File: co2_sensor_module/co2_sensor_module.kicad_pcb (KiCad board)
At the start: 2 copper layers, 85 x 55 mm, 59 parts, among them J1 Conn_ARM_SWD_TagConnect_TC203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, J2 Conn_01x04, J3 Conn_01x04, J4 Conn_01x03, J5 Conn_01x04, SW1 SW_DIP_x04, U1 SGX-7OX, U10 TPS62125DSG, U2 CBLW 24C02, U3 ADS1115IDGS, U4 TPS62125DSG, U5 MS5611-01BA, U6 SHT4x, U7 STC31-C, U8 TJA1042T-3, U9 STM32L432KBUx

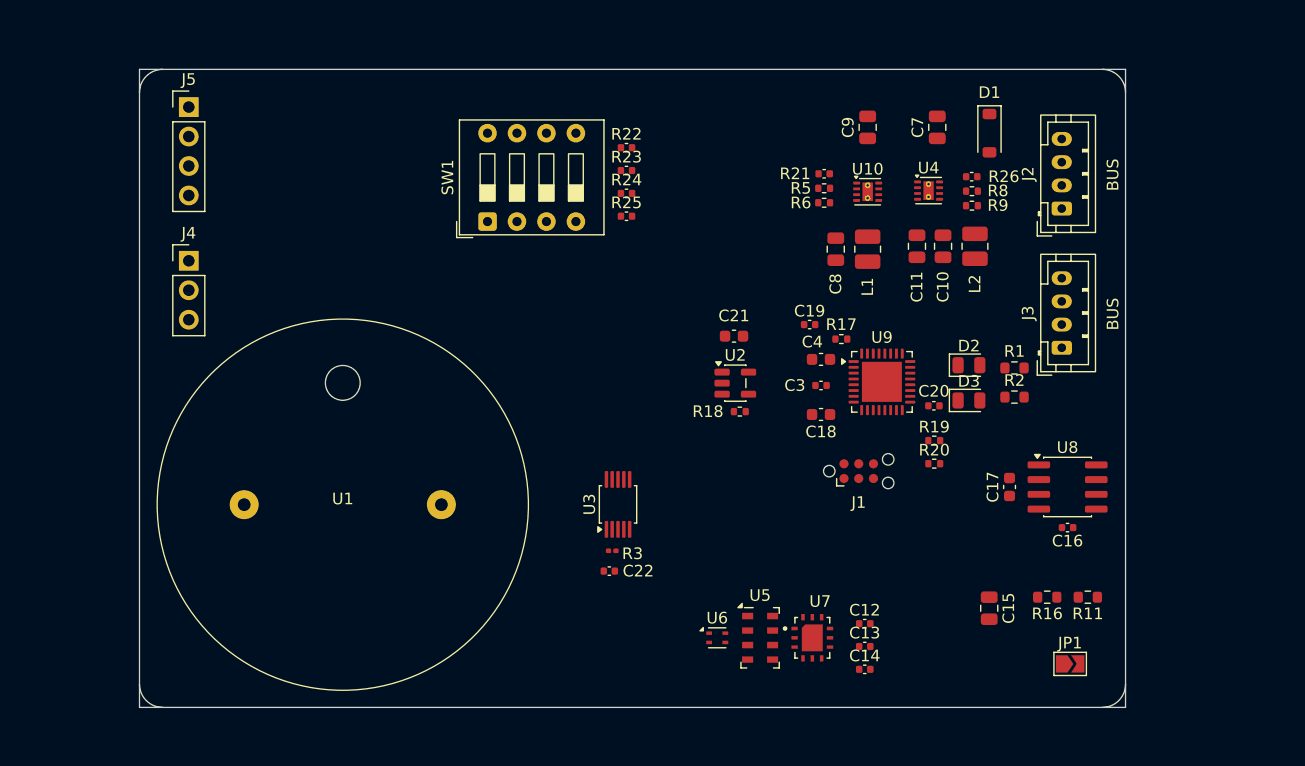
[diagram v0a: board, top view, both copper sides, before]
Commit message: some work on layout for co2 sensor unit
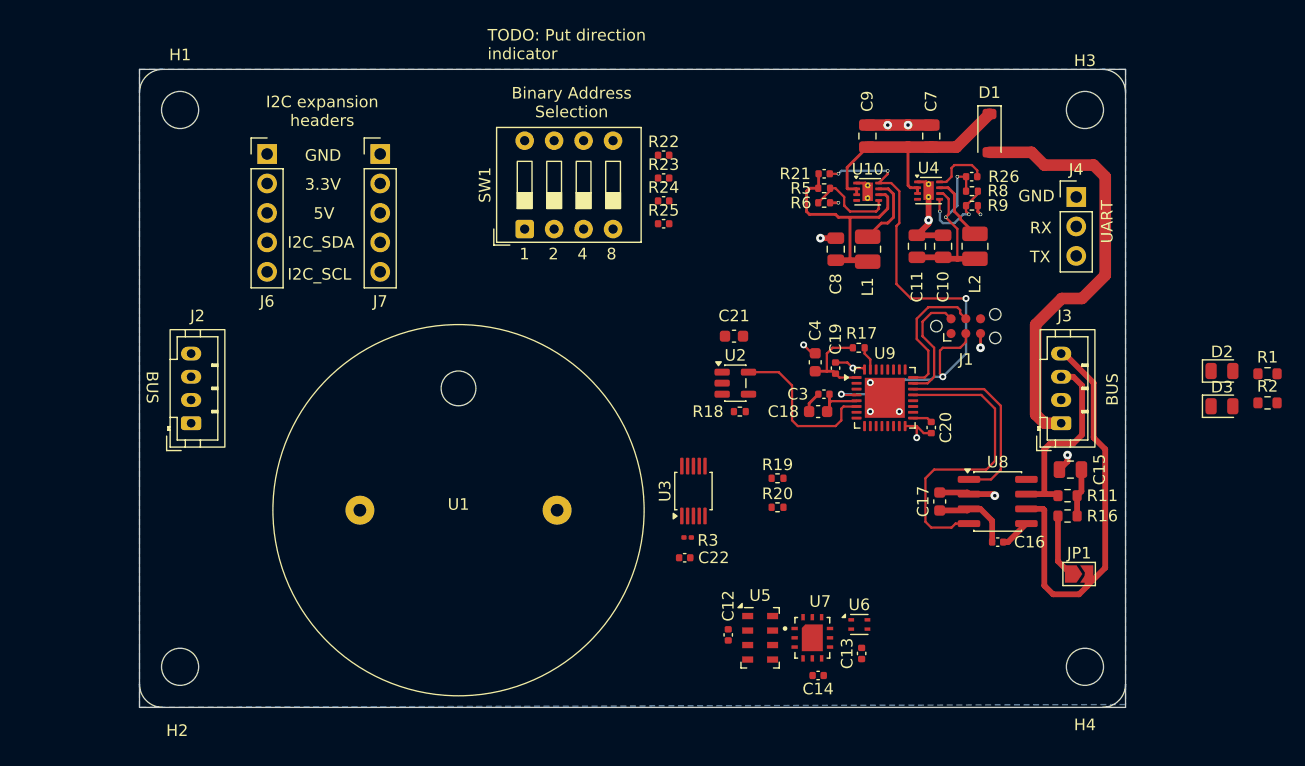
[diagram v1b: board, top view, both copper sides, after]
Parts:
- removed J5: Conn_01x04, Connector_PinHeader_2.54mm:PinHeader_1x04_P2.54mm_Vertical
- added H1: MountingHole 3M, MountingHole:MountingHole_3.2mm_M3, F.Cu at (99.5, 66.5)
- added H2: MountingHole 3M, MountingHole:MountingHole_3.2mm_M3, F.Cu at (99.5, 114.5)
- added H3: MountingHole 3M, MountingHole:MountingHole_3.2mm_M3, F.Cu at (177.5, 66.5)
- added H4: MountingHole 3M, MountingHole:MountingHole_3.2mm_M3, F.Cu at (177.5, 114.5)
- added J6: Conn_01x05, Connector_PinHeader_2.54mm:PinHeader_1x05_P2.54mm_Vertical, F.Cu at (107.0, 70.3)
- added J7: Conn_01x05, Connector_PinHeader_2.54mm:PinHeader_1x05_P2.54mm_Vertical, F.Cu at (116.8, 70.3)
- moved J2 77.3 mm to (100.5, 93.5)
- moved J4 76.7 mm to (176.8, 74.0)
- moved D2 21.8 mm to (189.3, 89.0)
- moved D3 21.8 mm to (189.3, 92.0)
- moved R1 21.8 mm to (193.2, 89.2)
- moved R2 21.8 mm to (193.2, 91.8)
- moved J1 15.5 mm to (167.2, 85.1)
- moved R20 14.0 mm to (151.0, 100.8)
- moved R19 13.9 mm to (151.0, 98.2)
- moved C15 13.8 mm to (176.2, 97.5), turned to 180 degrees
- moved U6 12.3 mm to (158.1, 110.8)
- moved C12 11.8 mm to (146.8, 111.8), turned to -90 degrees
- moved U1 9.99 mm to (123.5, 101.0)
- moved R11 8.92 mm to (176.0, 99.8), turned to 0 degrees
- moved JP1 7.79 mm to (177.0, 106.5)
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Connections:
- net /CAN/PV50 renamed /P5V0
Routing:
- net /MCU/~{nRST}: track 0.00 -> 47.1 mm, vias 0 -> 5
- net /Vbus: track 0.00 -> 37.4 mm
- net /P3V3: track 0.00 -> 36.1 mm
- net /CANL: track 0.00 -> 35.8 mm
- net /GND: track 0.00 -> 33.2 mm, vias 0 -> 15
- net /CAN/RX: track 0.00 -> 26.5 mm
- net /P5V0: track 0.00 -> 24.5 mm, vias 0 -> 2
- net /Power/Vbus: track 0.00 -> 22.0 mm
- net /CANH: track 0.00 -> 16.8 mm
- net /CAN/TX: track 0.00 -> 16.8 mm
- net Net-(U2-WP): track 0.00 -> 14.3 mm
- net /MCU/SWCLK: track 0.00 -> 11.8 mm
- net /MCU/SWDIO: track 0.00 -> 10.2 mm
- net Net-(U10-FB): track 0.00 -> 7.98 mm
- net Net-(U4-FB): track 0.00 -> 7.25 mm, vias 0 -> 2
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- added copper zone on B.Cu, net /GND
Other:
- board text added: "1"
- board text added: "2"
- board text added: "3.3V"
- board text added: "4"
- board text added: "5V"
- board text added: "8"
- board text added: "Binary Address Selection"
- board text added: "CANH"
- board text added: "CANL"
- board text added: "GND"
- board text added: "I2C expansion headers"
- board text added: "I2C_SCL"
- board text added: "I2C_SDA"
- board text added: "RX"
- board text added: "TODO: Put direction indicator"
- board text added: "TX"
- board text added: "UART"
- board text added: "VBUS"

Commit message: more routing
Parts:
- added C23: 100nF, Capacitor_SMD:C_0402_1005Metric, F.Cu at (148.4, 96.0)
- moved J2 72.0 mm to (169.7, 113.3), turned to 180 degrees
- moved R2 37.5 mm to (157.0, 101.5), turned to -90 degrees
- moved R1 35.9 mm to (159.5, 101.5), turned to -90 degrees
- moved D3 32.9 mm to (157.0, 98.0), turned to 90 degrees
- moved D2 31.1 mm to (159.5, 98.0), turned to 90 degrees
- moved R25 11.5 mm to (143.7, 65.1)
- moved R24 8.42 mm to (143.7, 66.3)
- moved C21 6.81 mm to (147.6, 92.8)
- moved C13 5.76 mm to (154.8, 108.8), turned to 90 degrees
- moved U6 5.69 mm to (152.8, 108.8)
- moved R23 5.47 mm to (143.7, 67.5)
- moved R19 5.27 mm to (151.5, 103.5), turned to 180 degrees
- moved R18 3.38 mm to (150.4, 90.4), turned to -90 degrees
- moved C14 3.24 mm to (156.8, 113.0), turned to -90 degrees
- moved R22 2.96 mm to (143.7, 68.8)
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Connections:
- U1 pad 2: Net-(U1-+) -> /GND
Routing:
- net /MCU/I2C_SDA: track 0.00 -> 127.7 mm, vias 0 -> 5
- net /MCU/I2C_SCL: track 0.00 -> 124.5 mm, vias 0 -> 7
- net /P5V0: track 24.5 -> 113.1 mm, vias 2 -> 4
- net /GND: track 33.2 -> 110.5 mm, vias 15 -> 26
- net Net-(U9-PB3): track 0.00 -> 52.5 mm, vias 0 -> 1
- net /P3V3: track 36.1 -> 86.6 mm, vias 0 -> 10
- net Net-(U9-PB4): track 0.00 -> 45.2 mm, vias 0 -> 1
- net Net-(U1-+): track 0.00 -> 38.8 mm
- net /CANL: track 35.8 -> 71.1 mm
- net /CANH: track 16.8 -> 48.0 mm
- net /Vbus: track 37.4 -> 67.4 mm
- net Net-(U9-PB0): track 0.00 -> 15.2 mm
- net Net-(U9-PB1): track 0.00 -> 12.7 mm
- net /CAN/STANDBY: track 0.00 -> 12.7 mm, vias 0 -> 2
- net Net-(D3-A): track 0.00 -> 4.96 mm
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- added copper zone on F.Cu, net /P3V3
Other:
- board text added: "+/ON"
- board text added: "0/OFF"
- board text added: "CAN end node"

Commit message: mostly done with sensor module
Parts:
- added C1: 0.1uF, Capacitor_SMD:C_0603_1608Metric, F.Cu at (157.5, 69.0)
- added C2: 0.1uF, Capacitor_SMD:C_0603_1608Metric, F.Cu at (168.0, 68.8)
- R3: footprint Resistor_SMD:R_0201_0603Metric -> Resistor_SMD:R_0603_1608Metric
- U10, U4: footprint Package_SON:Texas_DSG0008A_WSON-8-1EP_2x2mm_P0.5mm_EP0.9x1.6mm_ThermalVias -> Package_SON:Texas_DSG0008A_WSON-8-1EP_2x2mm_P0.5mm_EP0.9x1.6mm
- moved R8 5.36 mm to (162.5, 72.5), turned to 90 degrees
- moved R9 4.60 mm to (163.8, 72.5), turned to 90 degrees
- moved L1 3.97 mm to (155.5, 76.2)
- moved C8 3.83 mm to (152.8, 76.5), turned to -90 degrees
- moved R21 3.52 mm to (157.5, 74.5), turned to 90 degrees
- moved U10 3.45 mm to (155.5, 72.5), turned to -90 degrees
- moved C9 3.25 mm to (155.5, 68.8)
- moved R5 3.18 mm to (152.0, 72.2), turned to 90 degrees
- moved R6 2.86 mm to (153.2, 72.2), turned to 90 degrees
- moved L2 2.51 mm to (166.5, 76.2)
- moved R26 2.37 mm to (168.5, 74.5), turned to 90 degrees
- moved U4 2.22 mm to (166.0, 72.5), turned to -90 degrees
- moved C10 2.16 mm to (164.0, 76.5), turned to -90 degrees
- moved C11 2.16 mm to (161.8, 76.5), turned to -90 degrees
- moved C7 1.75 mm to (166.0, 68.8)
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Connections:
- R22 pad 1: Net-(U9-PB4) -> Net-(U9-PB3)
- R23 pad 1: Net-(U9-PB3) -> Net-(U9-PB4)
- R24 pad 1: Net-(U9-PB1) -> Net-(U9-PB5)
- R25 pad 1: Net-(U9-PB0) -> Net-(U9-PB6)
- SW1 pad 5: Net-(U9-PB4) -> Net-(U9-PB3)
- SW1 pad 6: Net-(U9-PB3) -> Net-(U9-PB4)
- SW1 pad 7: Net-(U9-PB1) -> Net-(U9-PB5)
- SW1 pad 8: Net-(U9-PB0) -> Net-(U9-PB6)
- U9 pad 14: Net-(U9-PB0) -> unconnected-(U9-PB0-Pad14)
- U9 pad 15: Net-(U9-PB1) -> unconnected-(U9-PB1-Pad15)
- U9 pad 28: unconnected-(U9-PB5-Pad28) -> Net-(U9-PB5)
- U9 pad 29: unconnected-(U9-PB6-Pad29) -> Net-(U9-PB6)
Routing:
- net Net-(U9-PB6): track 0.00 -> 56.1 mm, vias 0 -> 1
- net Net-(U9-PB5): track 0.00 -> 52.1 mm, vias 0 -> 1
- net /MCU/UART_TX: track 0.00 -> 37.2 mm, vias 0 -> 1
- net /MCU/UART_RX: track 0.00 -> 34.2 mm, vias 0 -> 1
- net /P3V3: track 86.6 -> 59.8 mm, vias 10 -> 4
- net /CANL: track 71.1 -> 55.3 mm
- net Net-(U9-PB0): track 15.2 -> 0.00 mm
- net Net-(U9-PB1): track 12.7 -> 0.00 mm
- net Net-(U9-PB3): track 52.5 -> 43.6 mm
- net /CANH: track 48.0 -> 40.1 mm, vias 0 -> 2
- net /MCU/~{nRST}: track 47.6 -> 39.9 mm, vias 5 -> 3
- net Net-(U10-FB): track 7.98 -> 3.44 mm
- net Net-(U10-SW): track 6.39 -> 1.88 mm
- net /GND: track 110.5 -> 114.4 mm, vias 26 -> 25
- net Net-(U4-FB): track 7.25 -> 3.34 mm, vias 2 -> 0
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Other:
- outline, holes or cut-outs redrawn
- board text removed: "TODO: Put direction indicator"

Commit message: (mostly) finalized sensing units + progress on surface hub
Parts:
- added C24: 100nF, Capacitor_SMD:C_0402_1005Metric, F.Cu at (140.5, 114.5)
- added C25: 1uF, Capacitor_SMD:C_0603_1608Metric, F.Cu at (138.5, 114.2)
- added U11: SGP41-D-R4, CustomFootprints:XDCR_SGP41-D-R4, F.Cu at (141.0, 112.0)
- moved U1 14.3 mm to (109.0, 100.8)
- moved H1 10.0 mm to (89.5, 66.5)
- moved H2 10.0 mm to (89.5, 114.5)
- moved J6 5.00 mm to (102.0, 69.5)
- moved C22 4.53 mm to (141.3, 102.9), turned to -90 degrees
- moved R3 2.92 mm to (142.6, 102.9), turned to -90 degrees
- moved J7 2.50 mm to (114.2, 69.5)
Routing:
- net /GND: track 114.4 -> 143.3 mm, vias 25 -> 28
- net /MCU/I2C_SCL: track 123.2 -> 138.7 mm, vias 7 -> 8
- net /MCU/I2C_SDA: track 125.7 -> 140.1 mm, vias 5 -> 6
- net /P3V3: track 59.8 -> 66.4 mm
- net Net-(U1-+): track 38.9 -> 44.8 mm
- net /P5V0: track 116.8 -> 121.8 mm
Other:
- board size 85 x 55 mm -> 95 x 55 mm
